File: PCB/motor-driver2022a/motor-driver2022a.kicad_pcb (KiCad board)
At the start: 2 copper layers, 72 x 54 mm, 56 parts, among them J1 Motor Power, J2 Logic Power, J3 Ch1 Input, J4 Ch2 Input, M1 Motor_DC, M2 Motor_DC, Q1 Q_PMOS_GDS, Q2 Q_NMOS_GDS, Q3 Q_PMOS_GDS, Q4 Q_NMOS_GDS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

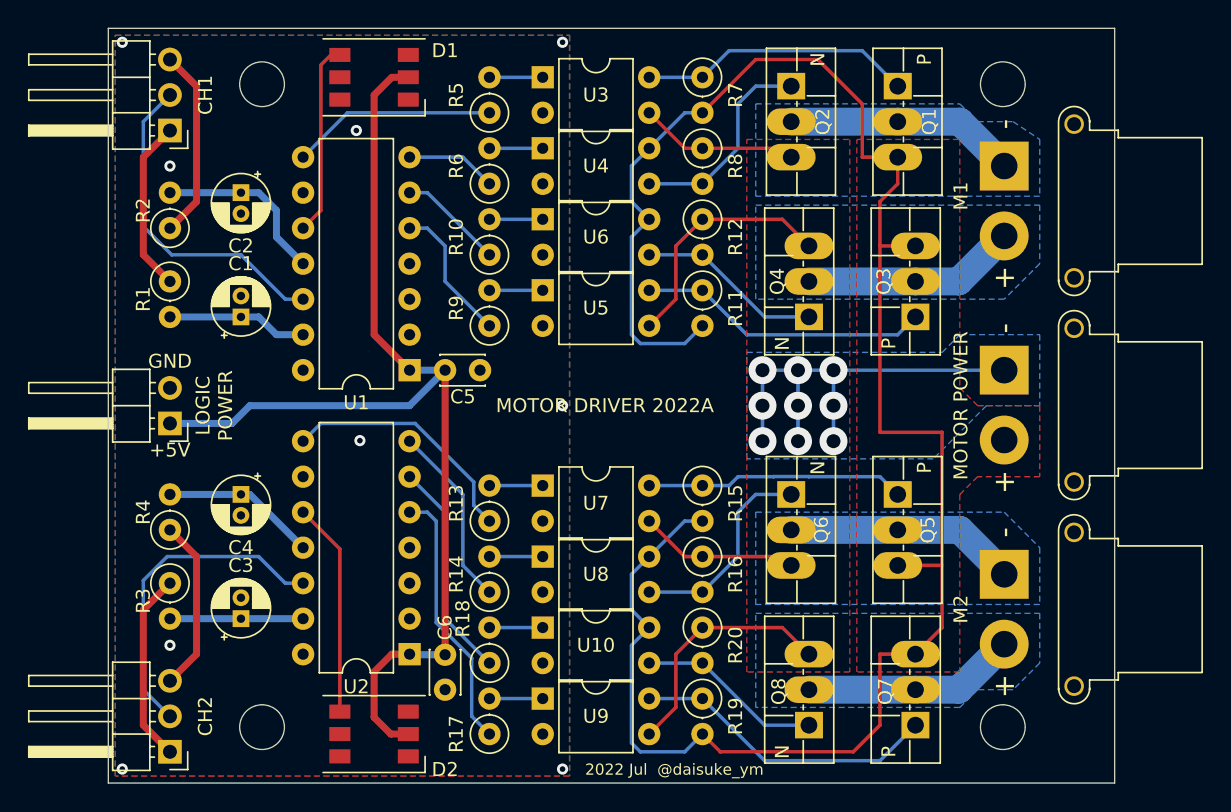
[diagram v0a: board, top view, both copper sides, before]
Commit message: ビアのサイズを変更 ビアを追加
git-svn-id: https://shiro-home.ddns.net/svn/project/motor-driver/trunk@43 73406841-da20-4056-b287-c5b29fcc9b8e
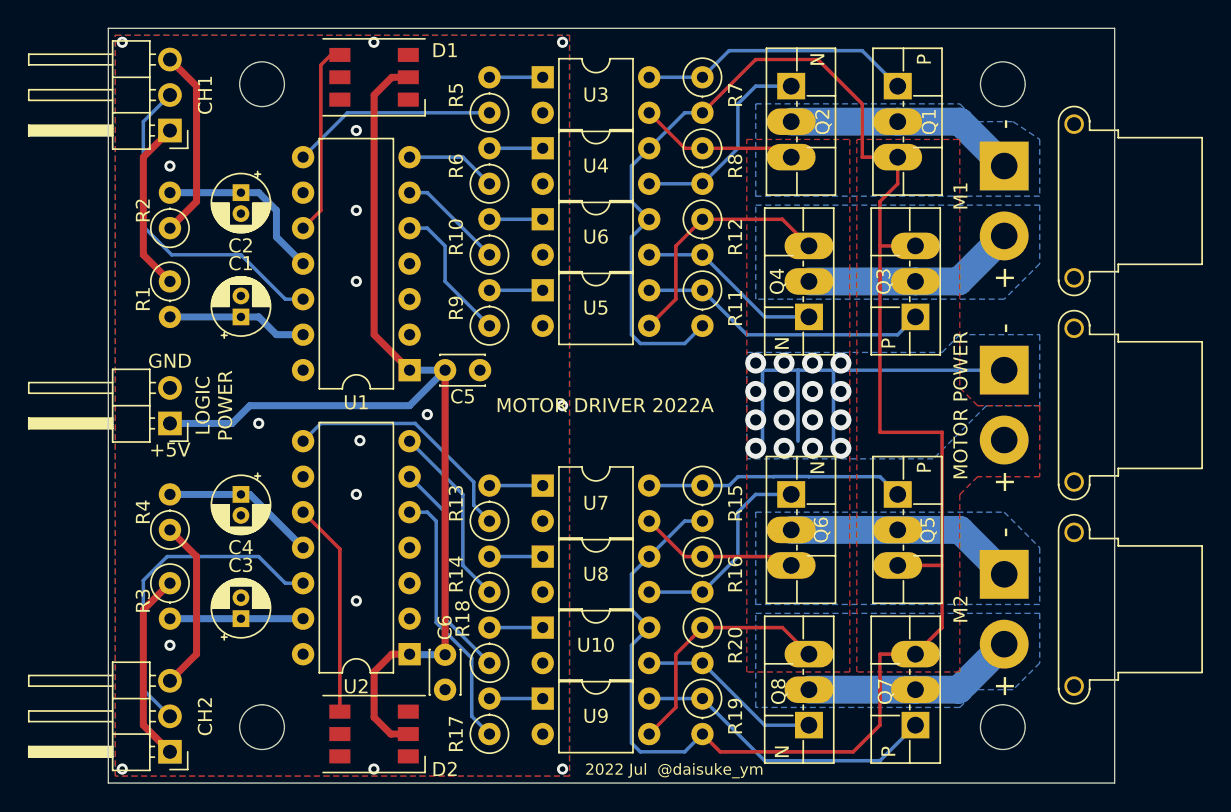
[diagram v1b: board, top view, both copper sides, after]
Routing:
- net GNDPWR: vias 9 -> 16
- net GND: vias 9 -> 17
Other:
- rule pad_to_mask_clearance: 0.05 -> 0
